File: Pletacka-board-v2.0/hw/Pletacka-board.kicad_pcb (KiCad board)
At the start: 2 copper layers, 29.7 x 87.4 mm, 41 parts, among them SW1 Reset_Button, SW2 User_Button, U1 TPS54231D, U2 EL357N(A)(TA)-G, U3 EL357N(A)(TA)-G

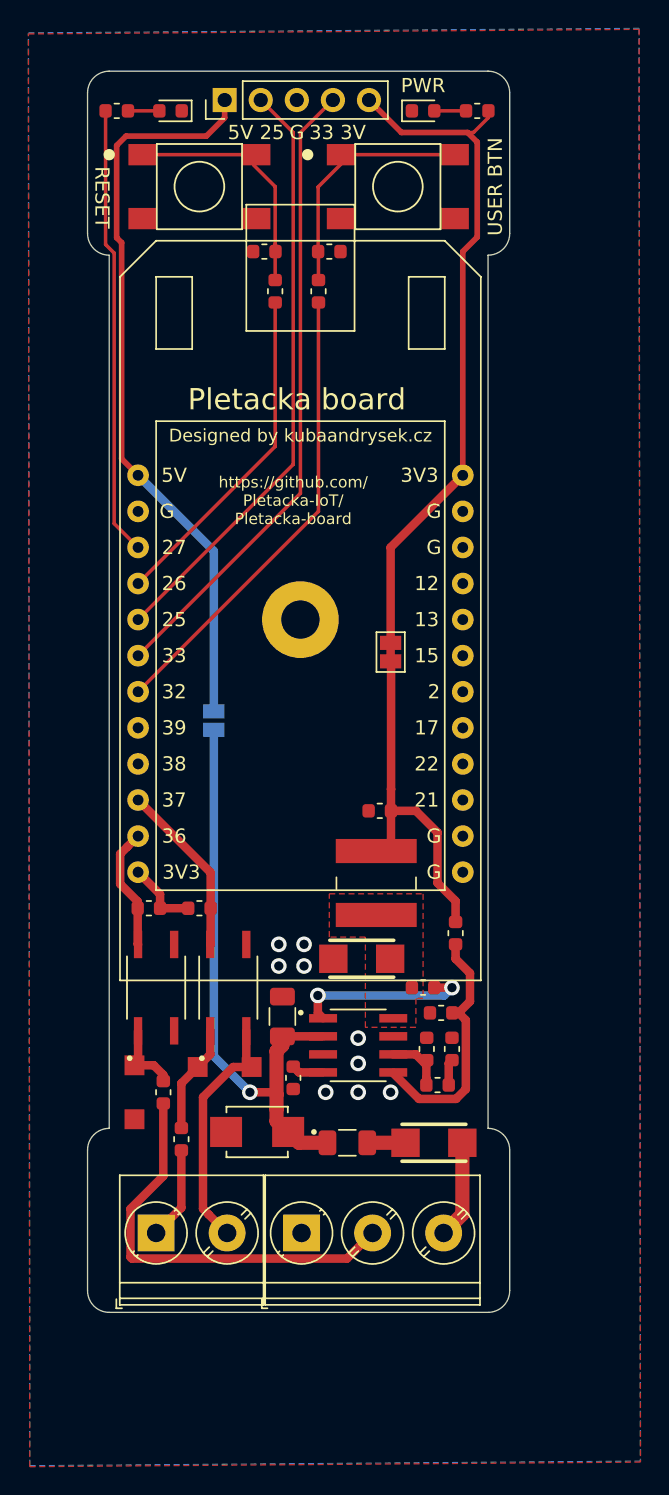
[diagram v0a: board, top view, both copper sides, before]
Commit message: Remove buttons - chage board
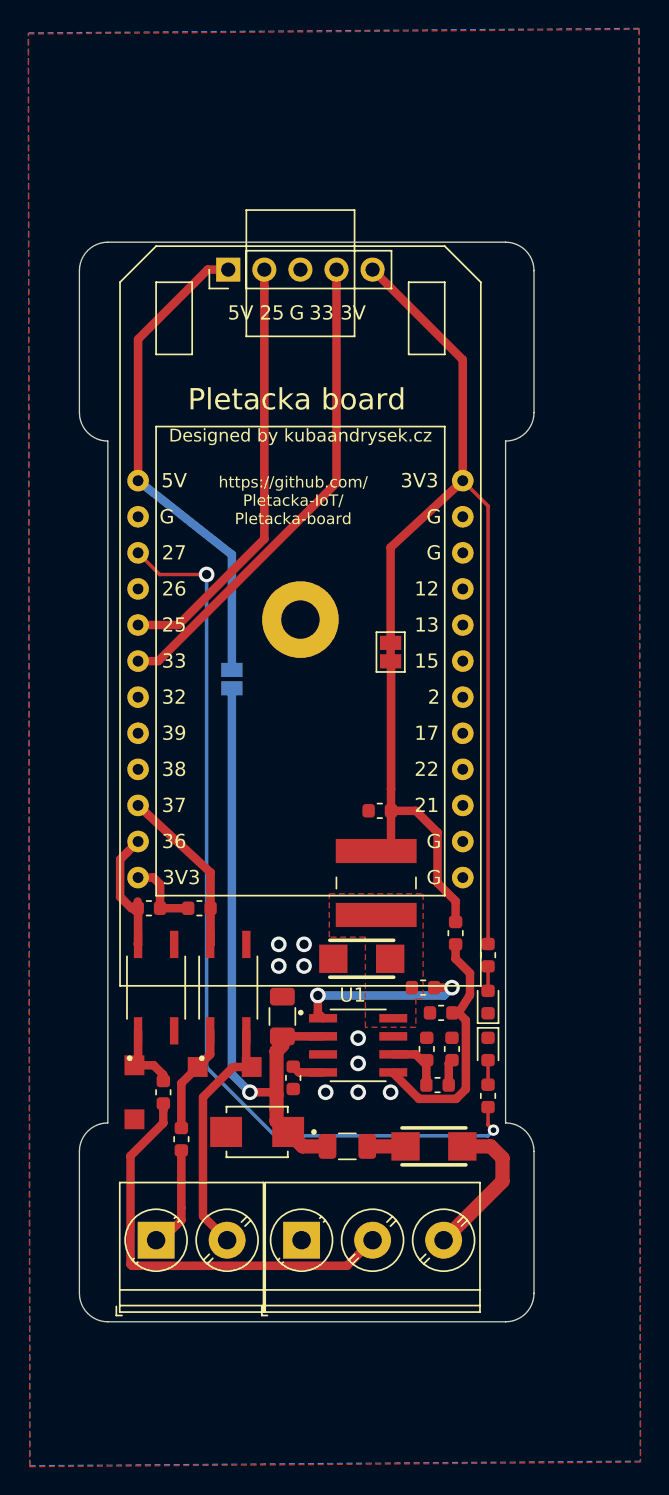
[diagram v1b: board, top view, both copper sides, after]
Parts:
- removed C7, C8: 100n, Capacitor_SMD:C_0603_1608Metric
- removed R8, R9: 2k2, Resistor_SMD:R_0603_1608Metric
- removed SW1: Reset_Button, Button_SMD:Button_SMD_10mm
- removed SW2: User_Button, Button_SMD:Button_SMD_10mm
- moved R2 74.1 mm to (159.8, 133.1), turned to 270 degrees
- moved D4 69.7 mm to (159.8, 129.8), turned to 270 degrees
- moved D3 62.9 mm to (159.8, 126.5), turned to 90 degrees
- moved R1 59.4 mm to (159.8, 123.2), turned to 90 degrees
- moved Pins1 11.9 mm to (141.5, 74.9)
- moved JP1 3.19 mm to (141.7, 103.8)
- moved POWER_&_FINN_INPUT1 0.51 mm to (146.6, 143.3)
- moved STOP_INPUT1 0.51 mm to (136.4, 143.3)
- moved ESP1 0.38 mm to (146.6, 99.9)
- moved D1 0.25 mm to (156.0, 136.7)
- moved POLYFUSE1 0.25 mm to (149.9, 136.7)
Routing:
- net BTN_USER: track 32.7 -> 0.00 mm
- net LED_USER: track 31.7 -> 64.3 mm, vias 0 -> 2
- net BTN_RESET: track 24.0 -> 0.00 mm
- net Net-(C8-Pad1): track 17.5 -> 0.00 mm
- net +5V: track 52.3 -> 34.9 mm
- net Net-(C7-Pad1): track 16.5 -> 0.00 mm
- net +3V3: track 53.8 -> 69.5 mm
- net USER_IO25: track 42.0 -> 30.4 mm
- net USER_IO33: track 44.8 -> 34.2 mm
- net VCC: track 6.90 -> 10.7 mm
- net Net-(C1-Pad1): track 41.5 -> 44.0 mm
- net OPTO_STOP_IN_PLUS: track 6.55 -> 7.28 mm
- net OPTO_STOP_IN_MINUS: track 17.3 -> 17.8 mm
- net OPTO_FINISHED_IN_PLUS: track 29.6 -> 30.1 mm
- net Net-(D3-Pad2): track 2.23 -> 1.73 mm
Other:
- board size 29.7 x 87.4 mm -> 32 x 76 mm
- board text removed: "PWR"
- board text removed: "RESET"
- board text removed: "USER BTN"
